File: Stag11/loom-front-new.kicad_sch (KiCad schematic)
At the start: 12 parts

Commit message: added loom stuff
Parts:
- removed Conn15: Deutsch_DTM_12S_Pin, symbol Connectors_SUFST:Deutsch_DTM_12S_Pin
- removed Conn16: Deutsch_DTM_6S_Pin, symbol Connectors_SUFST:Deutsch_DTM_6S_Pin
- removed Conn17: AMPHENOL-21P-Pannel, symbol Connectors_SUFST:AMPHENOL-21P-Pannel
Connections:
- net APPS1.SIG: no longer Conn13.7
- net APPS2.SIG: no longer Conn13.6
- net BMS.FAULT.LATCHING: no longer Conn13.9
- net BPS.FRONT.SIG: no longer Conn13.4
- net BPS.REAR.SIG: no longer Conn13.3
- net CAN.S.HIGH: no longer Conn13.14, Conn13.18
- net CAN.S.LOW: no longer Conn13.15, Conn13.19
- net COCKPIT.TS.LED.EXC: no longer Conn13.26
- net DASHBOX.EXC: now also Conn8.4; no longer Conn13.1
- net DASHBOX.GND: now also Conn8.34; no longer Conn13.2
- net IMD.FAULT.LATCHING: no longer Conn13.10
- net L120.ERX+: no longer Conn13.25
- net L120.ERX-: no longer Conn13.24
- net L120.ETX+: no longer Conn13.23
- net L120.ETX-: no longer Conn13.22
- net PEDALBOX.EXC: now also Conn8.1
- net PEDALBOX.GND: now also Conn8.2
- net RTDS.EXC: no longer Conn13.12
- net RTDS.GND: no longer Conn13.13
- net SAGL.EXC: now also Conn8.32; no longer Conn13.42
- net SAGL.GND: now also Conn8.31; no longer Conn13.43
- net SAGL.SIG: now also Conn8.30; no longer Conn13.5
- net TS.ON: no longer Conn13.11
- net TS.READY: no longer Conn13.8
- removed net CAN.C.HIGH: Conn13.16, Conn13.20, Conn8.20
- removed net CAN.C.LOW: Conn13.17, Conn13.21, Conn8.21
- net L120.ANALOGUE.TEMP.1: no longer names the net of Conn13.37
- net L120.ANALOGUE.TEMP.2: no longer names the net of Conn13.38
- net L120.ANALOGUE.VOLT.1: no longer names the net of Conn13.29
- net L120.ANALOGUE.VOLT.2: no longer names the net of Conn13.30
- net L120.ANALOGUE.VOLT.3: no longer names the net of Conn13.31
- net L120.ANALOGUE.VOLT.4: no longer names the net of Conn13.32
- net L120.ANALOGUE.VOLT.5: no longer names the net of Conn13.33
- net L120.ANALOGUE.VOLT.6: no longer names the net of Conn13.34
- net L120.DIGITAL.1: no longer names the net of Conn13.35
- net L120.DIGITAL.2: no longer names the net of Conn13.36
- net L120.SENSOR.5V.EXC: no longer names the net of Conn13.27
- net L120.SENSOR.GND: no longer names the net of Conn13.28
- net L120.SPEED.1: no longer names the net of Conn13.39
- net L120.SPEED.2: no longer names the net of Conn13.40
- net L120.SPEED.3: no longer names the net of Conn13.41
- no-connect marks 24 -> 19
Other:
- note added: "Terminate CAN at dash box?"
- note removed: "NORMALLY CAPPED OFF"
- moved on the sheet: Conn12, Conn14

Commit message: Completed LV and HV Box
TODO: Spec LV connectors
TODO: Add CAN-node to LV box
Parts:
- added Conn41: Deutsch_DTM_12S_Pin, symbol Connectors_SUFST:Deutsch_DTM_12S_Pin
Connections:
- net RS-232.GND is gone; now on net BPS.REAR.SIG: Conn8.24
- net RS-232.RX is gone; now on net APPS2.SIG: Conn8.22
- net RS-232.TX is gone; now on net APPS1.SIG: Conn8.23
- net BMS.FAULT.LATCHING: now also Conn8.8
- net BPS.FRONT.SIG: now also Conn8.25
- net BSPD.CUR_SEN.EXC: now also Conn8.28; no longer Conn8.27
- net BSPD.CUR_SEN.GND: now also Conn8.29; no longer Conn8.28
- net COCKPIT.TS_OFF.LED.GND: now also Conn8.7; no longer Conn8.29
- net CT.SIG: now also Conn8.3
- net IMD.FAULT.LATCHING: now also Conn8.9
- net RTDS.EXC: now also Conn8.20
- net RTDS.GND: now also Conn8.21
- net SPARE.EXC: now also Conn8.26; no longer Conn8.25
- net SPARE.GND: now also Conn8.27; no longer Conn8.26
- net TS.ON: now also Conn8.14
- net TS.READY: now also Conn8.13
- net TSAL.GREEN.LED.GND: now also Conn8.11
- net TSAL.LED.EXC: now also Conn8.10
- net TSAL.RED.LED.GND: now also Conn8.12
- net DASHBOX.EXC renamed DASH.EXC
- net DASHBOX.GND renamed DASH.GND
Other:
- note added: "Terminate CAN at dash?"
- note removed: "Terminate CAN at dash box?"
- moved on the sheet: Conn13

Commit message: updates
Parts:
- removed Conn13: AMPHENOL-47P-Pannel, symbol Connectors_SUFST:AMPHENOL-47P-Recepticle
- Conn41: value Deutsch_DTM_12S_Pin -> Molex 02x07; footprint (none) -> Connector_Molex:Molex_Micro-Fit_3.0_43045-1418_2x07-1MP_P3.00mm_Vertical; P/N TODO: ADD CONNECTOR - NEED ATLEAST 14 PINS -> Check connector - Molex 2x7
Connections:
- net BMS.FAULT.LATCHING: now also Conn41.9
- net CAN.S.HIGH: now also Conn41.4
- net CAN.S.LOW: now also Conn41.5
- net DASH.EXC: now also Conn41.1
- net DASH.GND: now also Conn41.2
- net IMD.FAULT.LATCHING: now also Conn41.10
- net R2D.BUTTON.GND: now also Conn41.14
- net TS.ON.BUTTON.GND: now also Conn41.13
- net R2D.LED.K: now reaches Conn41.12
- net DRS.BUTTON.GND: now reaches Conn41.7
- net IMD.LED.K: now reaches Conn41.8
- net TS.ON: no longer names the net of Conn8.14
- net TS.READY: no longer names the net of Conn8.13

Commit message: Front and Rear almost complete
TODO: Arrange power
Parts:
- removed Conn14: Deutsch_DTM_4S_Pin, symbol Connectors_SUFST:Deutsch_DTM_4S_Pin
- added Q1, Q2, Q3, Q4, Q5, Q6, Q7, Q8: 2N7002, Package_TO_SOT_SMD:SOT-23, symbol Transistor_FET:2N7002
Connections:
- net COCKPIT.TS.LED.GND is gone; now on net R2D.LED.K: Conn8.15
- net COCKPIT.TS_OFF.LED.GND is gone; now on net TSAL.LED.EXC: Conn8.7
- net LV.LED.EXC is gone; now on net IMD.LED.K: Conn8.17
- net LV.LED.GND is gone; now on net BMS.LED.K: Conn8.16
- net DRS.BUTTON.GND: now also Conn8.11
- net R2D.BUTTON.GND: now also Conn8.12
- net SAGL.EXC: no longer Conn8.32
- net SAGL.GND: no longer Conn8.31
- net TS.DETECTED.DASH.A: now also Conn41.10, Conn8.10
- net TS.ON.BUTTON.GND: now also Conn8.13
- net TSAL.GREEN.LED.GND: now also Conn8.8; no longer Conn8.11
- net TSAL.LED.EXC: no longer Conn8.10
- net TSAL.RED.LED.GND: now also Conn8.9; no longer Conn8.12
- net TSAL.GREEN.DASH.LED.K: now reaches Conn8.14
- net TSAL.GREEN.DASH.LED.K: now also Conn41.11
- net BMS.FAULT.LATCHING renamed BMS.LED.K
- net BMS.LED.K: no longer Conn8.8
- removed net IMD.FAULT.LATCHING: Conn41.10, Conn8.9
- new net: Q4.1 (G), Q7.3 (D)
- new net: Q3.2 (S), Q4.3 (D), Q7.2 (S)
- new net: Q2.2 (S), Q3.3 (D), Q8.2 (S)
- new net: Q3.1 (G), Q8.3 (D)
- new net: Q1.1 (G), Q5.2 (S)
- new net: Q1.2 (S), Q2.3 (D), Q6.3 (D)
- new net: Q2.1 (G), Q6.2 (S)
- new net SHUT_IN: Q1.3 (D), Q5.3 (D)
- new net SHUT_OUT: Q4.2 (S)
- no-connect marks 19 -> 22
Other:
- note added: "-->"
- note added: "Off Board"
- note removed: "NC at "DASH LEDs" conn"

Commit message: misc changes
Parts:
- removed Q1, Q2, Q3, Q4, Q5, Q6, Q7, Q8: 2N7002, Package_TO_SOT_SMD:SOT-23, symbol Transistor_FET:2N7002
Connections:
- net TSAL.GREEN.LED.GND renamed TSAL.GREEN.LED.K
- net TSAL.RED.LED.GND renamed TSAL.RED.LED.K
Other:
- note removed: "Off Board"

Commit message: I forgot what I did but changed CAN layout
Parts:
- added Conn65: Deutsch_DTM_2S_Pin, symbol Connectors_SUFST:Deutsch_DTM_2S_Pin
- added R9: 120, symbol Device:R_Small
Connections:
- net CAN.S.HIGH: now also Conn65.1, R9.1
- net CAN.S.LOW: now also Conn65.2, R9.2
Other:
- note added: "If including pressure sensor"
- note added: "Splice Power too?"

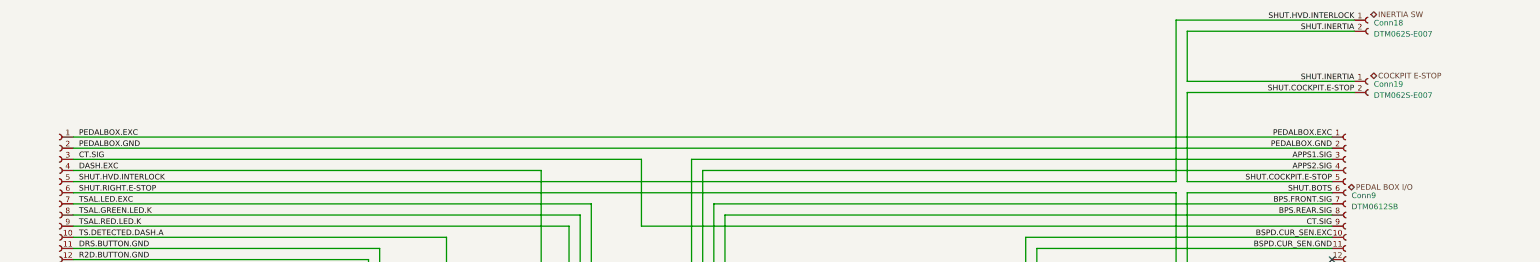
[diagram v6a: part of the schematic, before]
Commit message: Reordered shutdown loop and spliced power in LV box
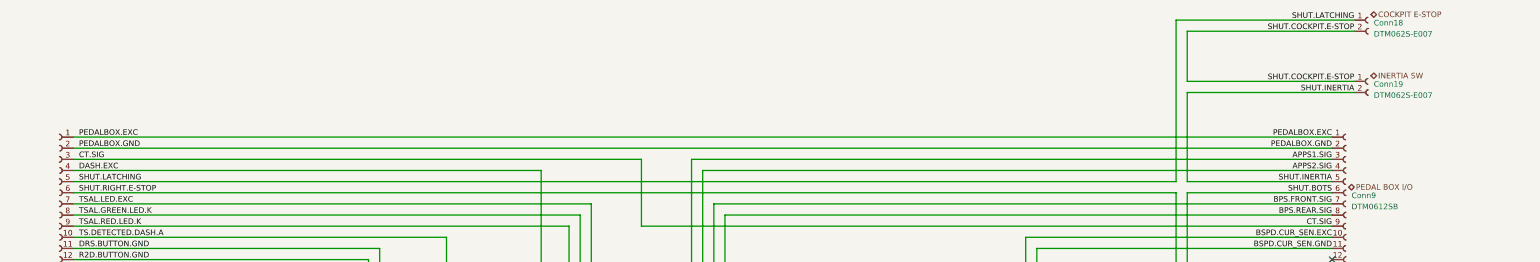
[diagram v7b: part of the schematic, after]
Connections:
- net SHUT.COCKPIT.E-STOP: now also Conn18.2, Conn19.1; no longer Conn19.2, Conn9.5
- net SHUT.INERTIA: now also Conn19.2, Conn9.5; no longer Conn18.2, Conn19.1
- net SHUT.HVD.INTERLOCK renamed SHUT.LATCHING
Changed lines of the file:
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@@
+		)
+	)
+	(label "SHUT.LATCHING"
+		(at 72.39 62.23 0)
+		(fields_autoplaced yes)
+		(effects
+			(font
+				(size 1.27 1.27)
+			)
+			(justify left bottom)
+		)
+	)
+	(label "SHUT.INERTIA"
+		(at 363.22 41.91 180)
+		(fields_autoplaced yes)
+		(effects
+			(font
+				(size 1.27 1.27)
+			)
+			(justify right bottom)
+		)
+	)
+	(label "SHUT.LATCHING"
+		(at 363.22 25.4 180)
+		(fields_autoplaced yes)
+		(effects
+			(font
+				(size 1.27 1.27)
+			)
+			(justify right bottom)
 		)
 	)
@@
 		)
 	)
-	(label "SHUT.COCKPIT.E-STOP"
-		(at 358.14 62.23 180)
-		(fields_autoplaced yes)
-		(effects
-			(font
-				(size 1.27 1.27)
-			)
-			(justify right bottom)
-		)
-	)
-	(label "SHUT.HVD.INTERLOCK"
-		(at 363.22 25.4 180)
-		(fields_autoplaced yes)
-		(effects
-			(font
-				(size 1.27 1.27)
-			)
-			(justify right bottom)
-		)
-	)
-	(label "SHUT.INERTIA"
-		(at 363.22 27.94 180)
-		(fields_autoplaced yes)
-		(effects
-			(font
-				(size 1.27 1.27)
-			)
-			(justify right bottom)
-		)
-	)
 	(label "TS.DETECTED.DASH.A"
 		(at 377.19 166.37 180)
@@
 		)
 	)
+	(label "SHUT.COCKPIT.E-STOP"
+		(at 363.22 27.94 180)
+		(fields_autoplaced yes)
+		(effects
+			(font
+				(size 1.27 1.27)
+			)
+			(justify right bottom)
+		)
+	)
 	(label "TS.DETECTED.DASH.A"
 		(at 72.39 74.93 0)
@@
 		)
 	)
+	(label "SHUT.COCKPIT.E-STOP"
+		(at 363.22 39.37 180)
+		(fields_autoplaced yes)
+		(effects
+			(font
+				(size 1.27 1.27)
+			)
+			(justify right bottom)
+		)
+	)
 	(label "PEDALBOX.EXC"
 		(at 72.39 52.07 0)
@@
 		)
 	)
-	(label "SHUT.HVD.INTERLOCK"
-		(at 72.39 62.23 0)
-		(fields_autoplaced yes)
-		(effects
-			(font
-				(size 1.27 1.27)
-			)
-			(justify left bottom)
-		)
-	)
 	(label "DRS.BUTTON.GND"
 		(at 377.19 158.75 180)
@@
 		)
 	)
-	(label "SHUT.COCKPIT.E-STOP"
-		(at 363.22 41.91 180)
-		(fields_autoplaced yes)
-		(effects
-			(font
-				(size 1.27 1.27)
-			)
-			(justify right bottom)
-		)
-	)
 	(label "R2D.LED.K"
 		(at 377.19 171.45 180)
@@
 		)
 	)
-	(label "SHUT.INERTIA"
-		(at 363.22 39.37 180)
-		(fields_autoplaced yes)
-		(effects
-			(font
-				(size 1.27 1.27)
-			)
-			(justify right bottom)
-		)
-	)
 	(label "SAGL.GND"
 		(at 97.79 118.11 0)
@@
 			)
 			(justify left bottom)
+		)
+	)
+	(label "SHUT.INERTIA"
+		(at 358.14 62.23 180)
+		(fields_autoplaced yes)
+		(effects
+			(font
+				(size 1.27 1.27)
+			)
+			(justify right bottom)
 		)
 	)
@@
 	(hierarchical_label "COCKPIT E-STOP"
 		(shape bidirectional)
-		(at 367.03 38.1 0)
+		(at 367.03 24.13 0)
 		(fields_autoplaced yes)
 		(effects
@@
 	(hierarchical_label "INERTIA SW"
 		(shape bidirectional)
-		(at 367.03 24.13 0)
-		(fields_autoplaced yes)
-		(effects
+		(at 367.03 38.1 0)
+		(fields_autoplaced yes)
+		(effects

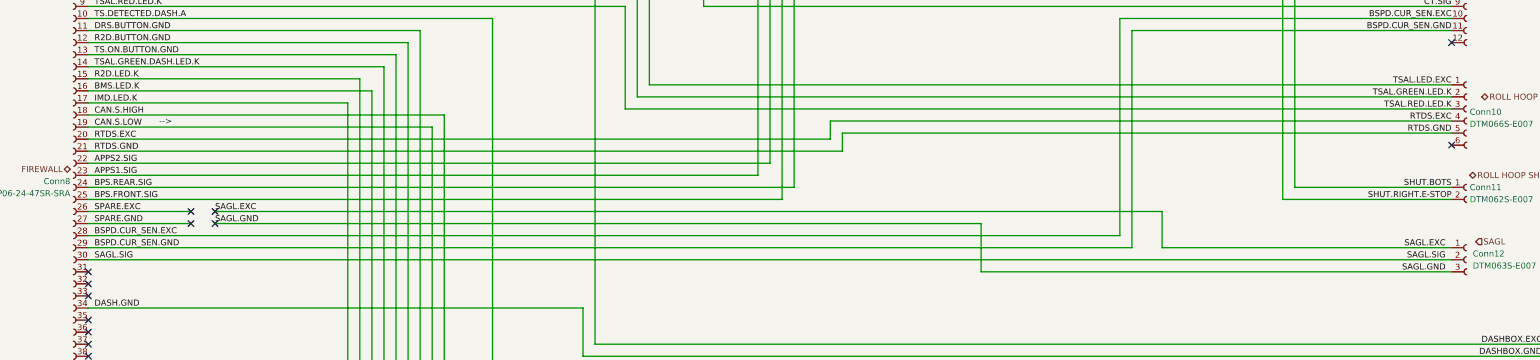
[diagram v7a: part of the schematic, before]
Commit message: Added TSAL+LATCHING board
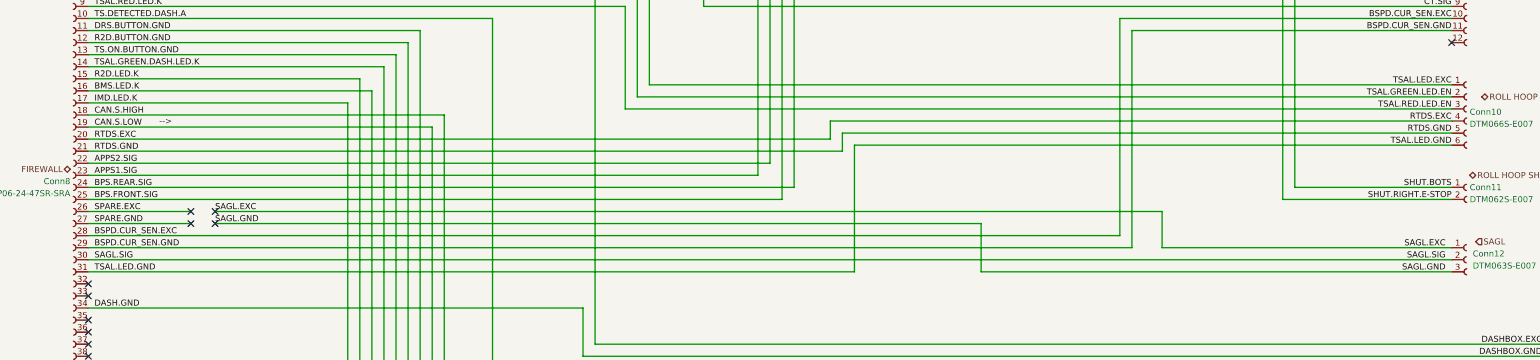
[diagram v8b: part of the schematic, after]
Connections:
- net TSAL.LED.GND: now reaches Conn10.6
- net TSAL.LED.GND: now also Conn8.31
- net TSAL.GREEN.LED.K renamed TSAL.GREEN.LED.EN
- net TSAL.RED.LED.K renamed TSAL.RED.LED.EN
- no-connect marks 22 -> 20
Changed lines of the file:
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@@
-	)
-	(no_connect
-		(at 71.12 128.27)
 	)
 	(no_connect
@@
 		(at 71.12 156.21)
 	)
-	(no_connect
-		(at 358.14 101.6)
-	)
 	(wire
 		(pts
@@
 	(wire
 		(pts
+			(xy 232.41 101.6) (xy 232.41 128.27)
+		)
+		(stroke
+			(width 0)
+			(type default)
+		)
+	)
+	(wire
+		(pts
 			(xy 146.05 95.25) (xy 146.05 151.13)
 		)
@@
 	(wire
 		(pts
+			(xy 358.14 101.6) (xy 232.41 101.6)
+		)
+		(stroke
+			(width 0)
+			(type default)
+		)
+	)
+	(wire
+		(pts
 			(xy 184.15 93.98) (xy 358.14 93.98)
 		)
@@
 		(pts
 			(xy 214.63 105.41) (xy 214.63 59.69)
+		)
+		(stroke
+			(width 0)
+			(type default)
+		)
+	)
+	(wire
+		(pts
+			(xy 232.41 128.27) (xy 71.12 128.27)
 		)
 		(stroke
@@
 		)
 	)
+	(label "TSAL.LED.GND"
+		(at 358.14 101.6 180)
+		(fields_autoplaced yes)
+		(effects
+			(font
+				(size 1.27 1.27)
+			)
+			(justify right bottom)
+		)
+	)
 	(label "SAGL.EXC"
 		(at 97.79 115.57 0)
@@
 		)
 	)
-	(label "TSAL.GREEN.LED.K"
+	(label "TSAL.GREEN.LED.EN"
 		(at 358.14 91.44 180)
 		(fields_autoplaced yes)
@@
 		)
 	)
-	(label "TSAL.RED.LED.K"
+	(label "TSAL.RED.LED.EN"
 		(at 358.14 93.98 180)
 		(fields_autoplaced yes)
@@
 		)
 	)
+	(label "TSAL.LED.GND"
+		(at 72.39 128.27 0)
+		(fields_autoplaced yes)
+		(effects
+			(font
+				(size 1.27 1.27)
+			)
+			(justify left bottom)
+		)
+	)
